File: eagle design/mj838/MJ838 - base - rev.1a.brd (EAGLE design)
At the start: 30 x 60 mm, 10 parts, among them J1 Vdc, J2 Dynamo, J3 CAN, J4 Battery, J5 FTSH-107-01-L-DV-K-A

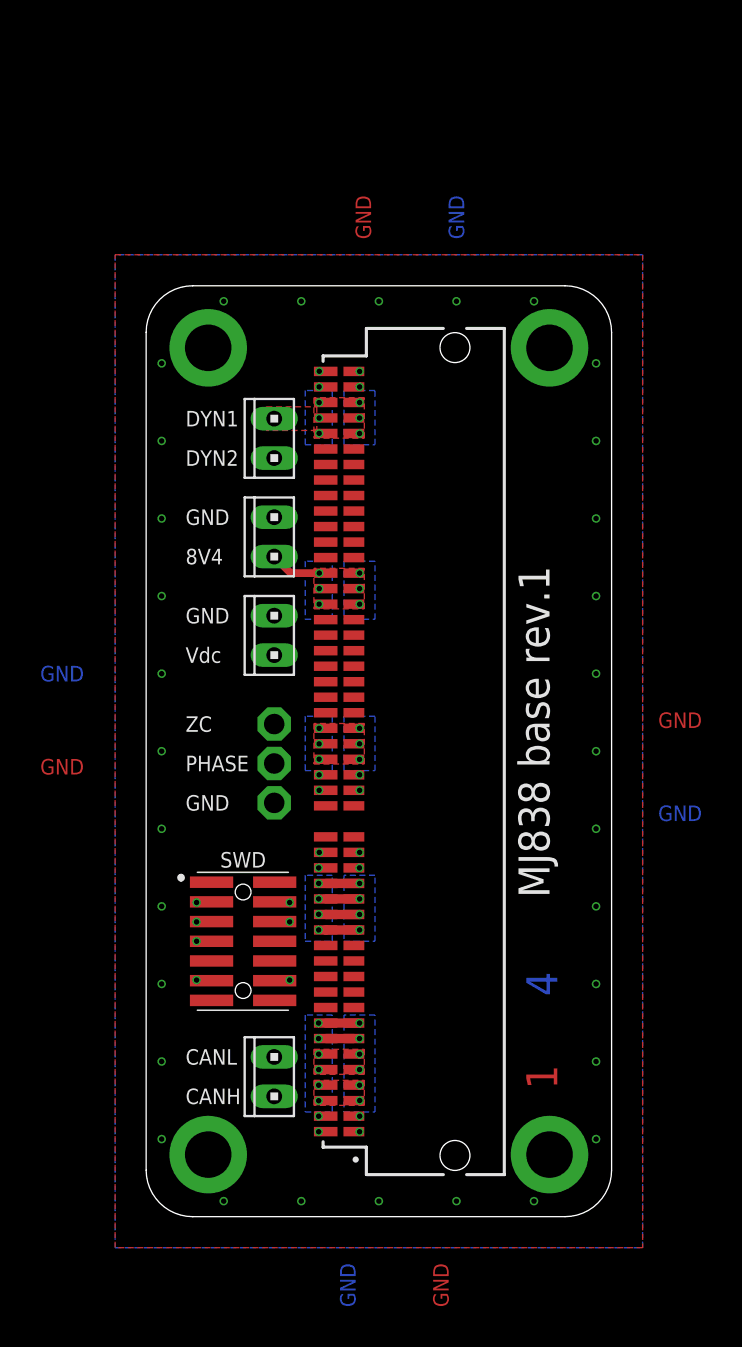
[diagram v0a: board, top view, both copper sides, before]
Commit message: in mj8x8.h: - prepared for SPI
in mj838.c/.h:
- preparation for sd card logger functionality
- adapted for I2C FeRAM IC change
- conversion to integer math:
-- scaled up wheel circumferences from floating point meters to integer millimeters: 2.350 became 2350
-- converted data members to integer
-- adapted algorithm to do computation in integer arithmetic and not floating point
- prepared for SPI
- removed PowerMonitorPower_Pin (was PB8) and created definition for general PB8_Pin GPIO
- started transfer from pac1952 objects towards ina219 objects

in adxl367.c/.h:
- continued driver development
- defined register addresses and sizes
- misc comment corrections
- added template for device driver

in autocharge.c:
- corrected speed value for SSR control
- fixed premature power off bug in _Do() where __AutoCharge._LEDDriver->Power() was called wrongly
- conversion to integer math:
-- converted data members to integer
-- adapted algorithm to do computation in integer arithmetic and not floating point
- started transfer from pac1952 objects towards ina219 objects
- modified code so that adjustable load does blink/not blink depending on speed

in zerocross.h, mj838_zerocross.c:
- added define to turn off zero cross frequency change rate calculation
- conversion to integer math:
-- converted data members to integer
-- adapted algorithm to do computation in integer arithmetic and not floating point
- moved __ZeroCross location to .data

in fm24cl.c./h:
- modified/renamed old mb85rc driver to work with new IC

in autodrive.c:
- in autodrive_ctor() added call to measure temperature/humidity at initialization

in i2c.c:
- as a temporary solution (until 1k pull-up resistors arrive), converted to pooling transfer functions and a 100kHz data transfer rate and built-in stm32 pull-up resistors
- activated high speed I2C, turned off internal pullups

in spi.c/.h:
- work on init function

in dac121c081.c:
- removed double declaration of __DAC121C081 object

in ina219.c:
- continued wo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
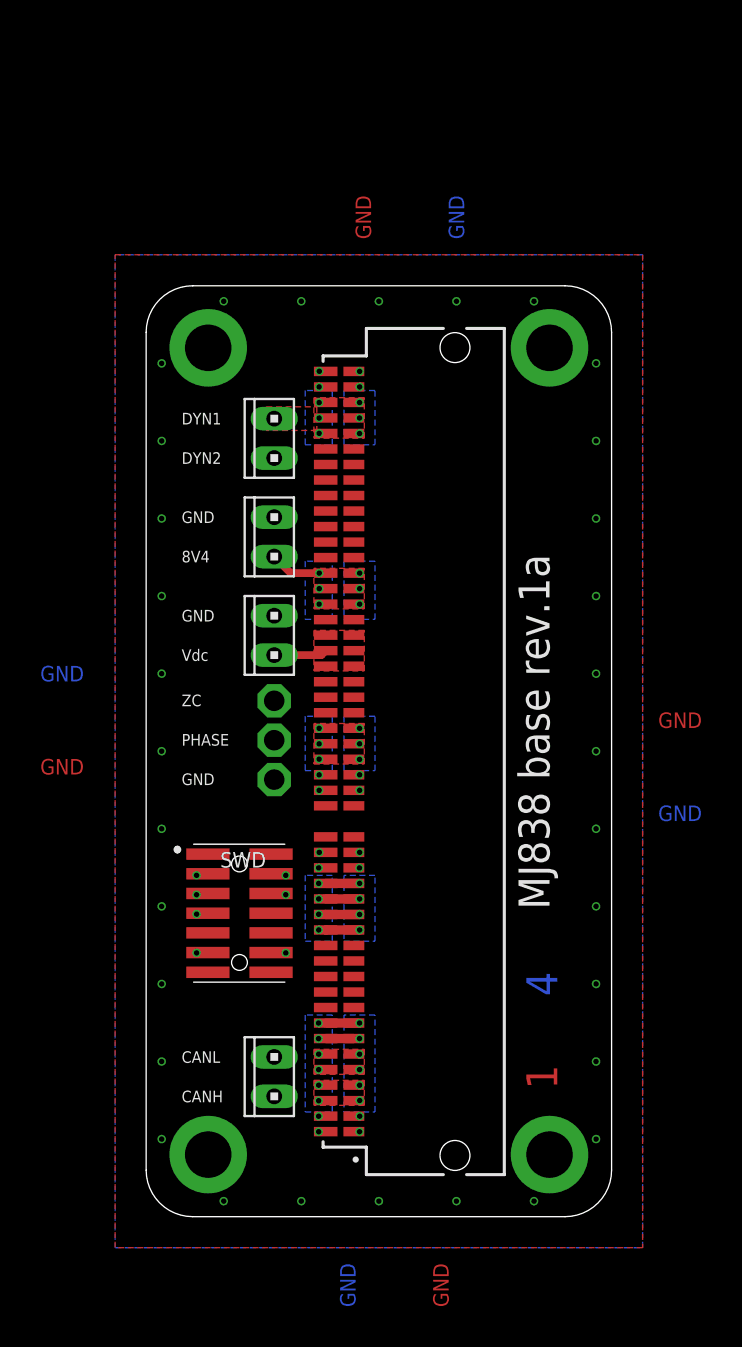
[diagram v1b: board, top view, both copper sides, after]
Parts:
- MARKER2: value (none) -> 4 Layer marker
- moved J5 1.83 mm to (6.01, 19.6)
- moved TP1 1.50 mm to (8.26, 28.2)
- moved TP2 1.50 mm to (8.26, 33.2)
- moved TP3 1.50 mm to (8.26, 30.7)
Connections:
- net VDC: now also CONN2.61, CONN2.62, CONN2.63, CONN2.64, CONN2.65, CONN2.66
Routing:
- net VDC: track 0.00 -> 3.44 mm
- net PHASE: track 24.4 -> 27.7 mm
- net SYS_NRST: track 8.44 -> 6.71 mm
- net SYS_SWDIO: track 7.85 -> 8.65 mm
- net SYS_SWCLK: track 7.97 -> 8.55 mm
- added copper zone on layer 1, net VDC
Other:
- board text added: "MJ838 base rev.1a"
- board text removed: "MJ838 base rev.1"

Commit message: finished HR30_6R_6PD(71) - FFC layout.brd & .sch this item allows for FFC connectivity between the base board and external connectors. the FFC has a pitch-out of 1mm (FFC width of 11mm) and mates with a HR30_6R_6PD(71) TH receptacle and a Samtecc FC1-10-02-T-WT FFC connector.
finished MJ838 - base - rev.1a.brd
this item is an improved version of the original base board.
it now can accept either the RA or straight version of the MEC1-150-02 card edge connector.
this board can be connected via wires or via the above HR30_6R_6PD(71) - FFC layout.brd.
for wired connection terminal blocks are used, for FFC connection a Samtec FC1-10-02-T-WT is used.
!!! these rev.1 base boards are NOT COMPATIBLE with earlier boards !!!

finished MJ838 - rev.1c.brd & .sch
this item is the next revision of the MJ838 device.
it follows a dual-device design started with rev.1b - the schematic/board are developed to support both mj838 and mj000 devices, depending on which firmware is loaded and which components are populated.
major improvements for mj838/mj000 in respect to rev.1b:
- far more powerful MCU (STM32L4P5CGU6) - more flash/ram, floating point, SDMMC, QSPI
- improved zerocross detection via TLV6703DDCR's internal refernece voltage
- addition of numerous TVS protection elements (SWD, ZC & phase signals, SDMMC interface)
- addition of the ADXL367 - Accelerometer for improved motion detection
- addition of QSPI for MRAM storage
- switch from SPI to SDMMC for interfacing SD Card storage
- addition of RN4678 bluetooth module (via UART) for wireless data transfer
- improved routing of MJ8x8 power bus, application load lines to card edge (and into base board) so that prod<->dev card swap is far easier
- addition of NFET controlled application/adjustable load switch

added old boards for reference; their name prefix is "reference - *"
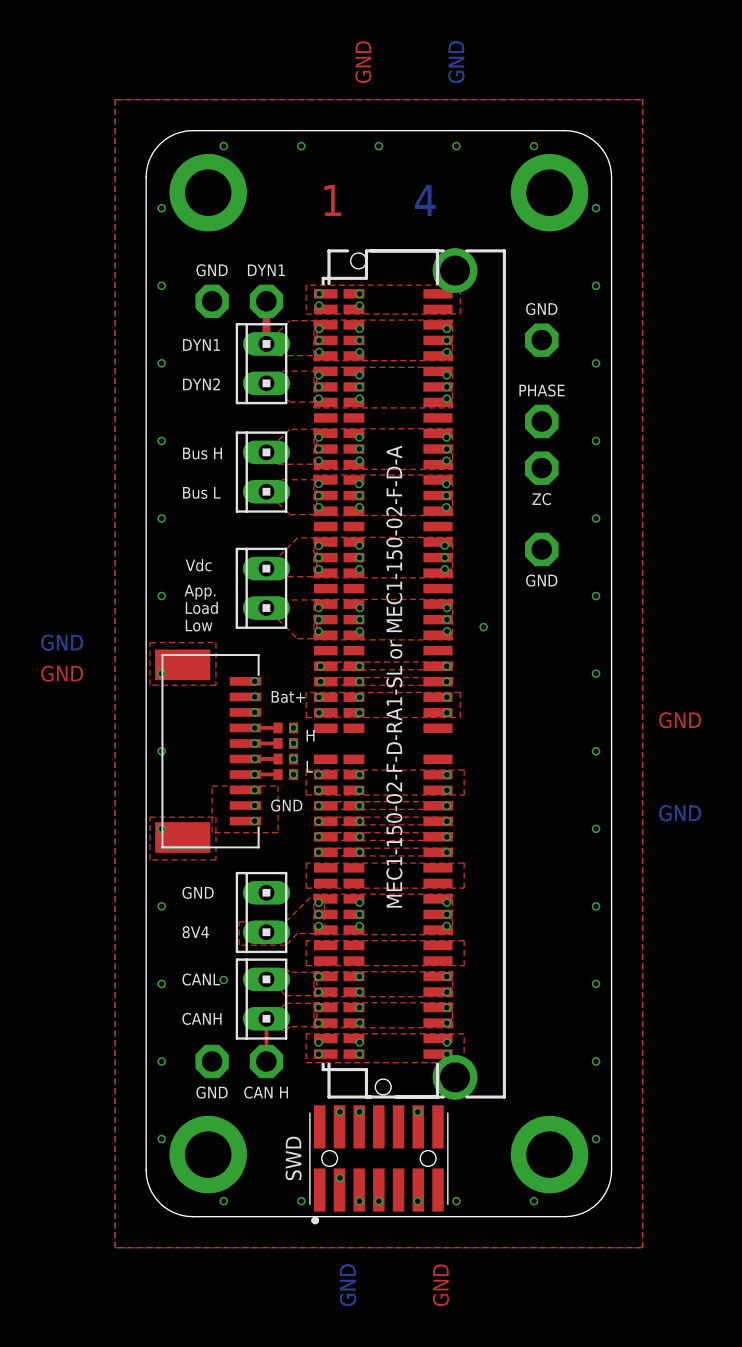
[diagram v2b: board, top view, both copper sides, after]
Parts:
- removed J1: Vdc, con-amp:10X02MTA
- added CONN3: FC1-10-02-T-WT, FC1-10-02-T - FFC Connector:SMD
- added J6, J7: Vdc, con-amp:10X02MTA
- added R1, R2, R3, R4: 0R, rcl:R0402
- added TP4, TP5, TP6, TP8, TP9: TPPAD1-13, testpad:P1-13
- CONN2: device Samtec MEC1 - Card Edge Connector:SAMTEC_MEC1-150-2-F-D-RA1 -> MEC1-150-X-X-D-RA1-SL-X:MEC1-150-02-F-D-COMBINED
- moved MARKER2 59.3 mm to (11.0, 65.5), turned to 0 degrees
- moved TP1 33.2 mm to (25.5, 56.5)
- moved TP3 26.8 mm to (25.5, 51.2)
- moved J4 24.2 mm to (7.75, 19.6)
- moved TP2 22.9 mm to (25.5, 48.2)
- moved J5 18.2 mm to (15.0, 3.75), turned to 0 degrees
- moved J3 5.02 mm to (7.75, 14.0)
- moved J2 4.84 mm to (7.75, 55.0)
- moved CONN2 2.87 mm to (16.1, 29.9)
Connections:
- new net APP_LOW: CONN2.55, CONN2.57, CONN2.59, CONN2.R55, CONN2.R57, CONN2.R59, CONN2.S56, CONN2.S58, CONN2.S60, J7.2
- new net MJ8X8_8V4_H: CONN2.77, CONN2.79, CONN2.81, CONN2.R77, CONN2.R79, CONN2.R81, CONN2.S78, CONN2.S80, CONN2.S82, J6.1
- new net MJ8X8_8V4_L: CONN2.71, CONN2.73, CONN2.75, CONN2.R71, CONN2.R73, CONN2.R75, CONN2.S72, CONN2.S74, CONN2.S76, J6.2
- new net N$1: CONN3.P$4, R1.2
- new net N$2: CONN3.P$5, R2.2
- new net N$3: CONN3.P$6, R3.2
- new net N$4: CONN3.P$7, R4.2
- net 3V3: now also CONN2.R33, CONN2.S34; no longer CONN2.34
- net BAT+: now also CONN2.17, CONN2.19, CONN2.21, CONN2.R17, CONN2.R19, CONN2.R21, CONN2.S18, CONN2.S20, CONN2.S22, CONN3.P$10, CONN3.P$8, CONN3.P$9; no longer CONN2.69, CONN2.70, CONN2.71, CONN2.72, CONN2.73, CONN2.74
- net CAN_H: now also CONN2.R05, CONN2.R07, CONN2.S06, CONN2.S08, R3.1, R4.1, TP6.TP; no longer CONN2.06, CONN2.08
- net CAN_L: now also CONN2.R09, CONN2.R11, CONN2.S10, CONN2.S12, R1.1, R2.1; no longer CONN2.10, CONN2.12
- net DYNAMO1: now also CONN2.R91, CONN2.R93, CONN2.R95, CONN2.S92, CONN2.S94, CONN2.S96, TP5.TP; no longer CONN2.92, CONN2.94, CONN2.96
- net DYNAMO2: now also CONN2.85, CONN2.87, CONN2.89, CONN2.R85, CONN2.R87, CONN2.R89, CONN2.S86, CONN2.S88, CONN2.S90; no longer CONN2.49, CONN2.50, CONN2.51, CONN2.52, CONN2.53, CONN2.54
- net GND: now also CONN2.13, CONN2.15, CONN2.23, CONN2.25, CONN2.53, CONN2.61, CONN2.69, CONN2.83, CONN2.R01, CONN2.R03, CONN2.R13, CONN2.R15, CONN2.R23, CONN2.R25, CONN2.R35, CONN2.R37, CONN2.R45, CONN2.R47, CONN2.R53, CONN2.R61, CONN2.R69, CONN2.R83, CONN2.R97, CONN2.R99, CONN2.S02, CONN2.S04, CONN2.S100, CONN2.S14, CONN2.S16, CONN2.S24, CONN2.S26, CONN2.S36, CONN2.S38, CONN2.S46, CONN2.S48, CONN2.S54, CONN2.S62, CONN2.S70, CONN2.S84, CONN2.S98, CONN3.GND1, CONN3.GND2, CONN3.P$1, CONN3.P$2, CONN3.P$3, TP4.TP, TP8.TP, TP9.TP; no longer CONN2.02, CONN2.04, CONN2.100, CONN2.36, CONN2.38, CONN2.46, CONN2.48, CONN2.98, J1.1
- net PHASE: now also CONN2.51, CONN2.R51, CONN2.S52; no longer CONN2.15, CONN2.16
- net SYS_NRST: now also CONN2.R27, CONN2.S28; no longer CONN2.28
- net SYS_SWCLK: now also CONN2.R29, CONN2.S30; no longer CONN2.30
- net SYS_SWDIO: now also CONN2.R31, CONN2.S32; no longer CONN2.32
- net VDC: now also CONN2.67, CONN2.R63, CONN2.R65, CONN2.R67, CONN2.S64, CONN2.S66, CONN2.S68, J7.1; no longer CONN2.61, CONN2.62, CONN2.64, CONN2.66, J1.2
- net ZEROCROSS: now also CONN2.49, CONN2.R49, CONN2.S50; no longer CONN2.13, CONN2.14
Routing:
- net CAN_H: track 2.98 -> 58.8 mm, vias 4 -> 8
- net CAN_L: track 2.94 -> 32.7 mm, vias 4 -> 8
- net BAT+: track 3.76 -> 26.8 mm, vias 6 -> 12
- net SYS_NRST: track 6.71 -> 24.1 mm, vias 3 -> 4
- net 3V3: track 15.9 -> 29.4 mm, vias 3 -> 4
- net SYS_SWDIO: track 8.65 -> 20.6 mm, vias 3 -> 4
- net SYS_SWCLK: track 8.55 -> 19.5 mm, vias 3 -> 4
- net ZEROCROSS: track 33.1 -> 27.8 mm, vias 2 -> 3
- net VDC: track 3.44 -> 0.00 mm, vias 0 -> 9
- net DYNAMO1: track 0.00 -> 2.75 mm, vias 6 -> 9
- net N$4: track 0.00 -> 2.70 mm, vias 0 -> 1
- net N$3: track 0.00 -> 2.70 mm, vias 0 -> 1
- net N$2: track 0.00 -> 2.70 mm, vias 0 -> 1
- net N$1: track 0.00 -> 2.70 mm, vias 0 -> 1
- net PHASE: track 27.7 -> 27.1 mm, vias 2 -> 3
- added copper zone on layer 1, net 3V3
- added copper zone on layer 1, net APP_LOW
- added copper zone on layer 1, net MJ8X8_8V4_H
- added copper zone on layer 1, net MJ8X8_8V4_L
- added copper zone on layer 1, net PHASE
- added copper zone on layer 1, net SYS_NRST
- added copper zone on layer 1, net SYS_SWCLK
- added copper zone on layer 1, net SYS_SWDIO
- added copper zone on layer 1, net ZEROCROSS
- removed copper zone on layer 2, net DYNAMO2
- removed copper zone on layer 15, net EXCL
- removed copper zone on layer 16, net EXCL
- removed copper zone on layer 2, net EXCL
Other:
- board size 30 x 60 mm -> 30 x 70 mm
- board text added: "App. Load Low"
- board text added: "Bat+"
- board text added: "Bus H"
- board text added: "Bus L"
- board text added: "CAN H"
- board text added: "H"
- board text added: "L"
- board text added: "MEC1-150-02-F-D-RA1-SL or MEC1-150-02-F-D-A"
